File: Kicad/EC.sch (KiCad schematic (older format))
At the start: 19 parts, among them U1 OP AMP

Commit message: updated after 8/25 feedback
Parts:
- removed D?: DIODE, ~, symbol DIODE
- removed R?: 100K, ~, symbol R
- removed R?: 47K, ~, symbol R
- removed U1, U? (x2): OP AMP, ~, symbol MCP6241
- added D?: DIODE, ~, symbol DIODE
- added R?: 100K, ~, symbol R
- added R?: 47K, ~, symbol R
- added R?: 10K, ~, symbol R
- added R?: 1K, ~, symbol R
- added U?: MCP6244, ~, symbol MCP6244
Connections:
- wire segments 62 -> 78
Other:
- note added: "Convert the peak of the EC Sine Wave to Digital Value\n"
- note added: "Generate Low Distortion Sine Wave"
- note added: "Not used"
- note added: "Read EC Probe"
- note removed: "*1"
- note removed: "*1 TBD: Op Amp for Wien Bridge Oscillator"
- note removed: "*2"
- note removed: "*2 See ? in 8/25 Build Notes"
- note removed: "generate Low Distortion Sine Wave"
- note removed: "read Conductivity Level"
- note removed: "turn into DC Signal"
- moved on the sheet: C?, D?, R?

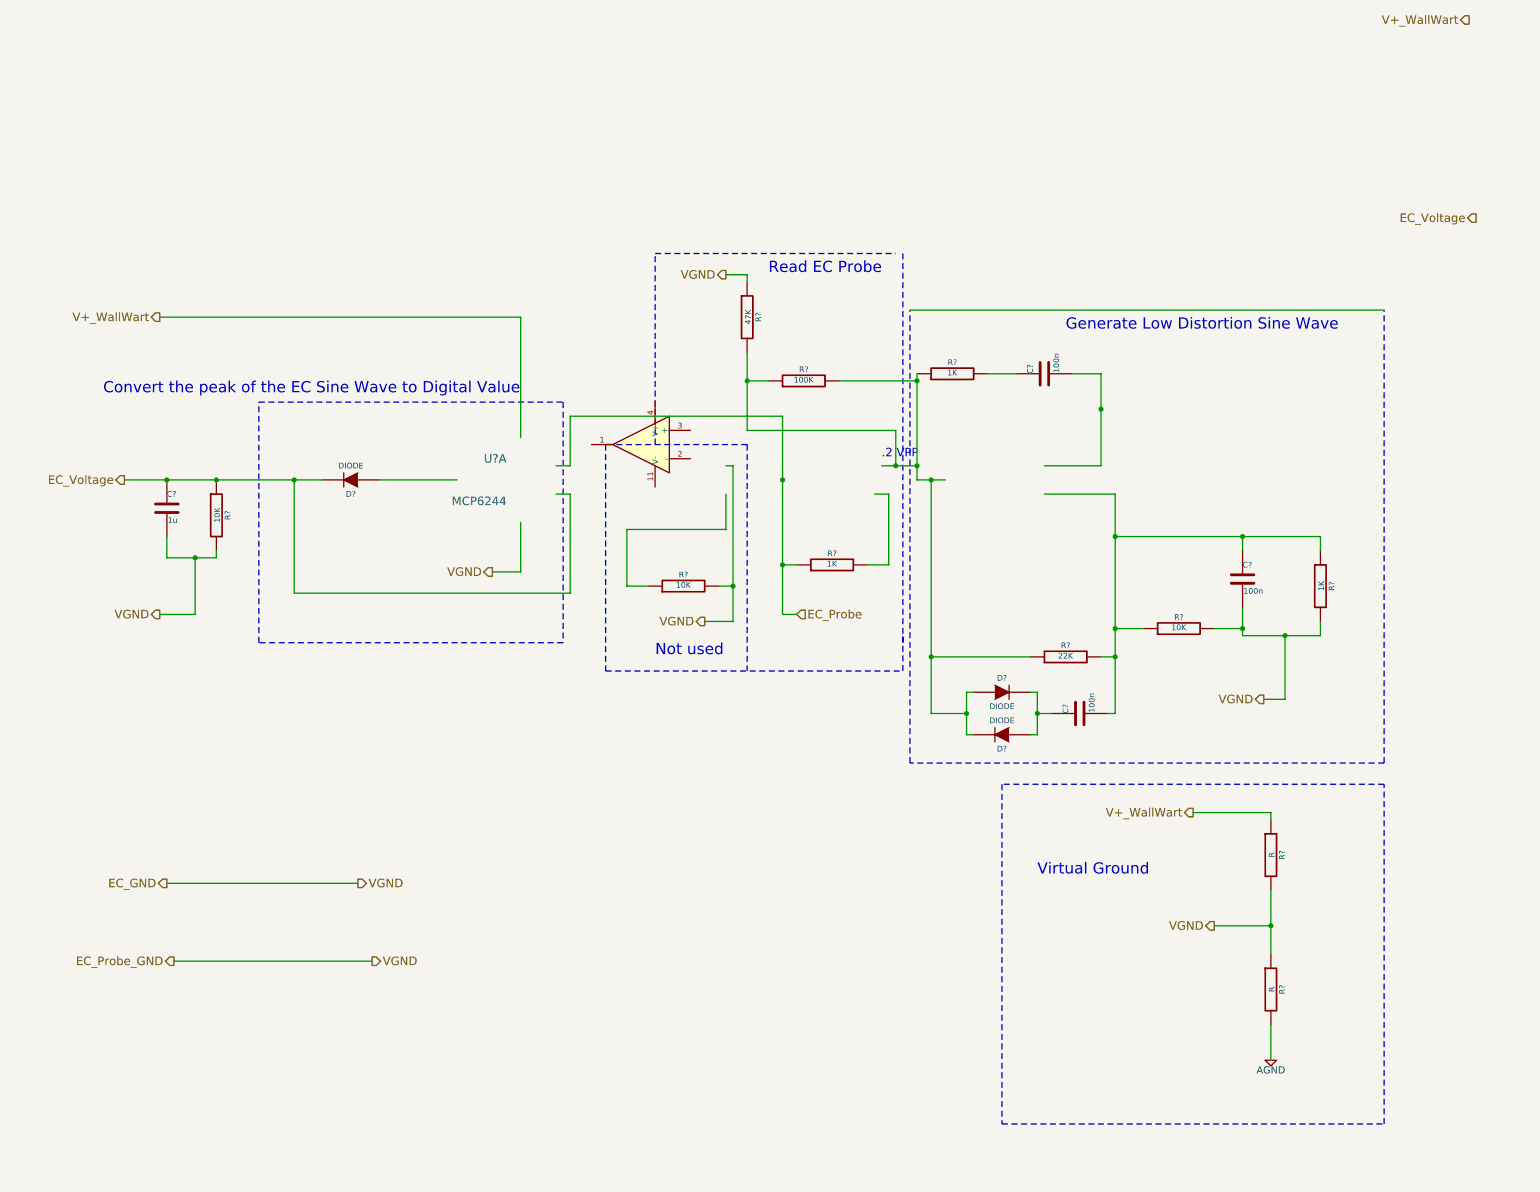
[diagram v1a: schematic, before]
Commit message: updated EC circuit
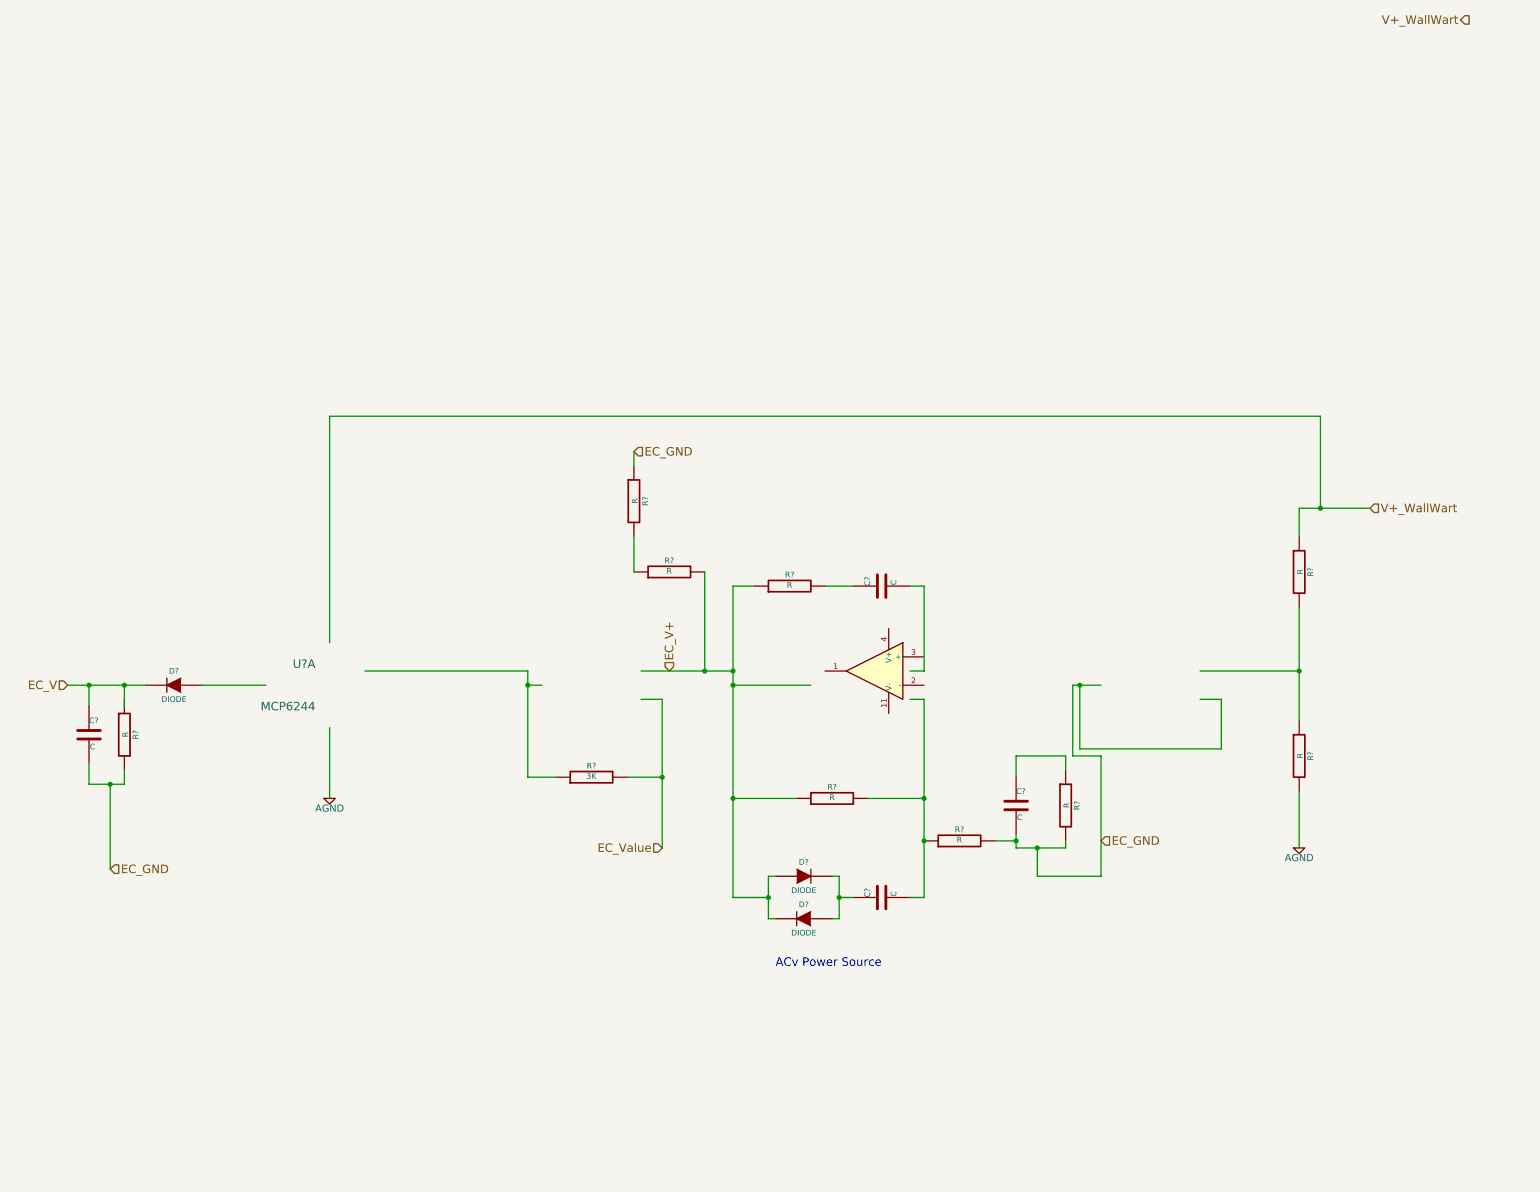
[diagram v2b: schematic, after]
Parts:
- removed C? (x3): 100n, ~, symbol C
- removed C?: 1u, ~, symbol C
- removed D? (x3): DIODE, ~, symbol DIODE
- removed R? (x3): 1K, ~, symbol R
- removed R? (x3): 10K, ~, symbol R
- removed R?: 22K, ~, symbol R
- removed R? (x2): R, ~, symbol R
- removed R?: 100K, ~, symbol R
- removed R?: 47K, ~, symbol R
- removed U?: MCP6244, ~, symbol MCP6244
- added C? (x4): C, ~, symbol C
- added D? (x3): DIODE, ~, symbol DIODE
- added R? (x9): R, ~, symbol R
- added R?: 3K, ~, symbol R
- added U?: MCP6244, ~, symbol MCP6244
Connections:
- net labels added: EC_V, EC_V+, EC_Value
- net labels removed: EC_Probe, EC_Probe_GND, EC_Voltage, VGND
- wire segments 78 -> 65
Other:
- note added: "ACv Power Source"
- note removed: ".2 VPP"
- note removed: "Convert the peak of the EC Sine Wave to Digital Value\n"
- note removed: "Generate Low Distortion Sine Wave"
- note removed: "Not used"
- note removed: "Read EC Probe"
- note removed: "Virtual Ground"

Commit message: Ready for 1st Review
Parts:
- removed U?: MCP6244, ~, symbol MCP6244
- added TP? (x8): CONN_1, symbol CONN_1
- added U? (x4): MCP6244, ~, symbol MCP6244
- C? (x3): value C -> 100n
- C?: value C -> 1u
- R? (x4): value R -> 1K
- R? (x2): value R -> 10K
- R?: value R -> 22K
- R?: value R -> 47K
- R?: value R -> 100K
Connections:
- net labels added: AC_Signal, EC_Probe+, EC_Probe-, EC_Signal
- net labels removed: EC_V+, EC_Value
- wire segments 65 -> 85
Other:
- note added: "2.5V"
- note added: "Convert AC to DC"
- note added: "Create an AC Signal"
- note added: "Get EC Measurement"
- note added: "Probe"
- note added: "Raise GND"
- note added: "Shrink Signal"
- note added: "Wien Bridge Oscillator"
- note removed: "ACv Power Source"
- moved on the sheet: C?, D?, R?

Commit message: Ready for Review
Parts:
- removed TP? (x3): CONN_1, symbol CONN_1
- removed U? (x4): MCP6244, ~, symbol MCP6244
- added U1: MCP6244, ~, symbol MCP6244
- gave numbers to parts that had none: 22
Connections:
- wire segments 85 -> 74

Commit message: Ready for layout review
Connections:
- net at D4.1 (A), D5.2 (K), R14.1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: now also R13.2, TP20.1, U1.7
- net AC_Signal renamed AC_Shrunk
- net EC_GND renamed VGND
- net EC_V renamed EC_Meas
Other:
- moved on the sheet: C10, C11, C3, C9, D3, D4, D5, R10, R11, R12, R13, R14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
